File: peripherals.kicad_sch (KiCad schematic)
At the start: 34 parts, among them U2 AT7456E, U3 TXU0304PWR, U4 ICM-42688-P, U5 MT29F2G01ABAGDWB-IT_G, U6 DPS310XTSA1, Y2 27MHz

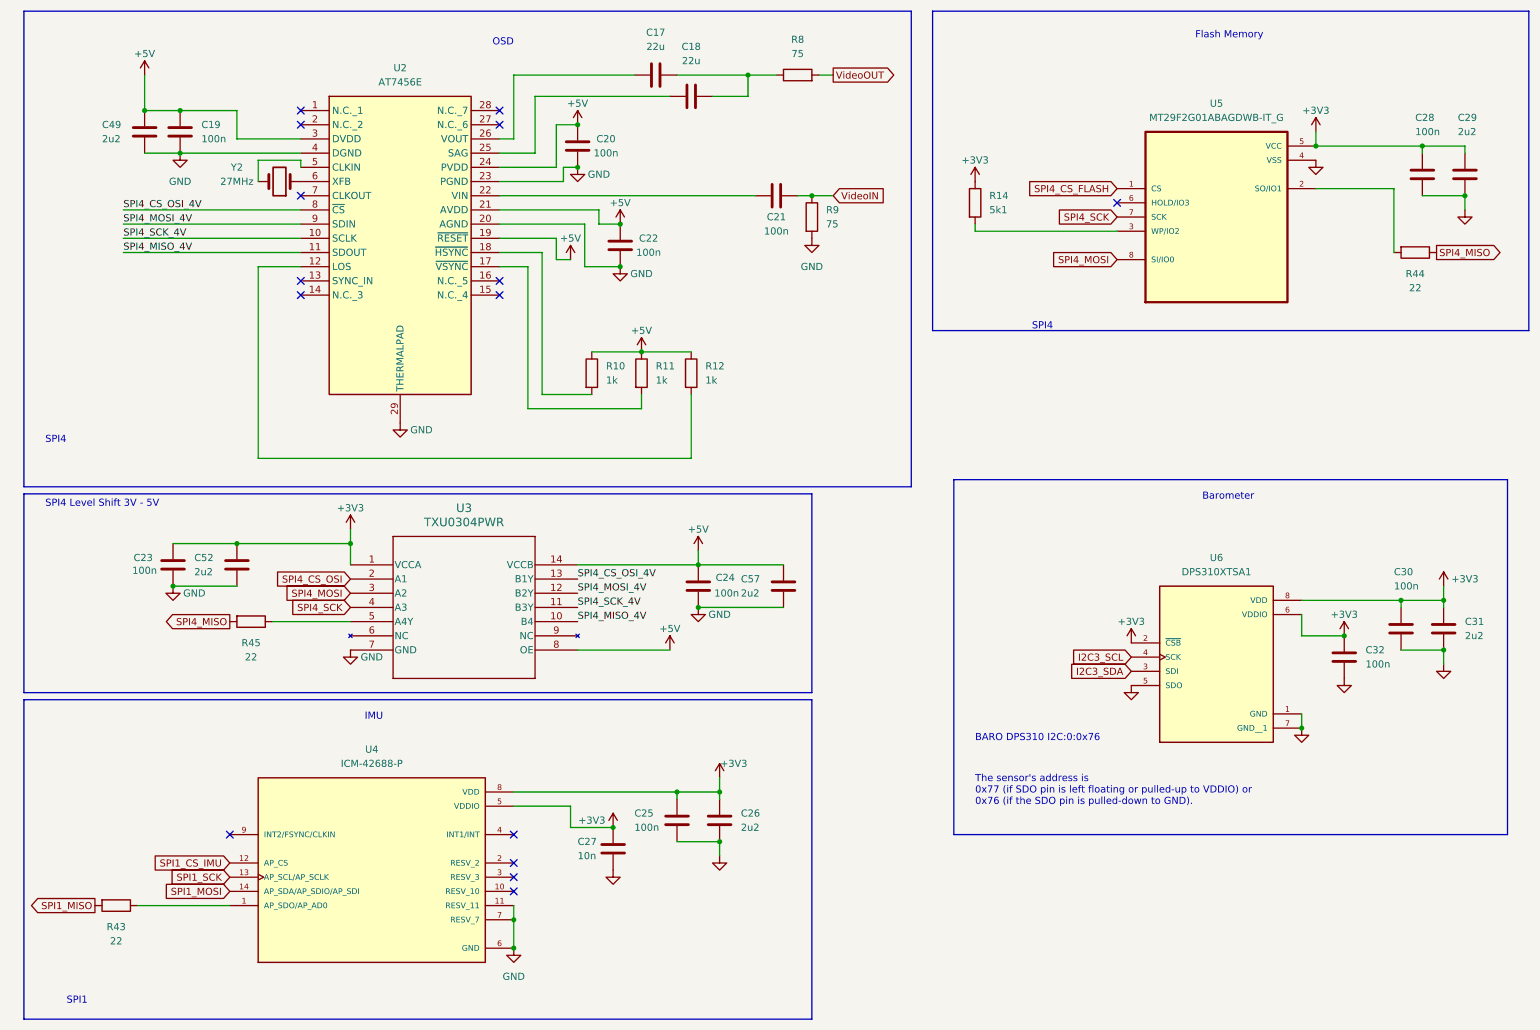
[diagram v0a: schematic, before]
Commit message: change flash to sd flash, cleanup, and reconcile with F405FC
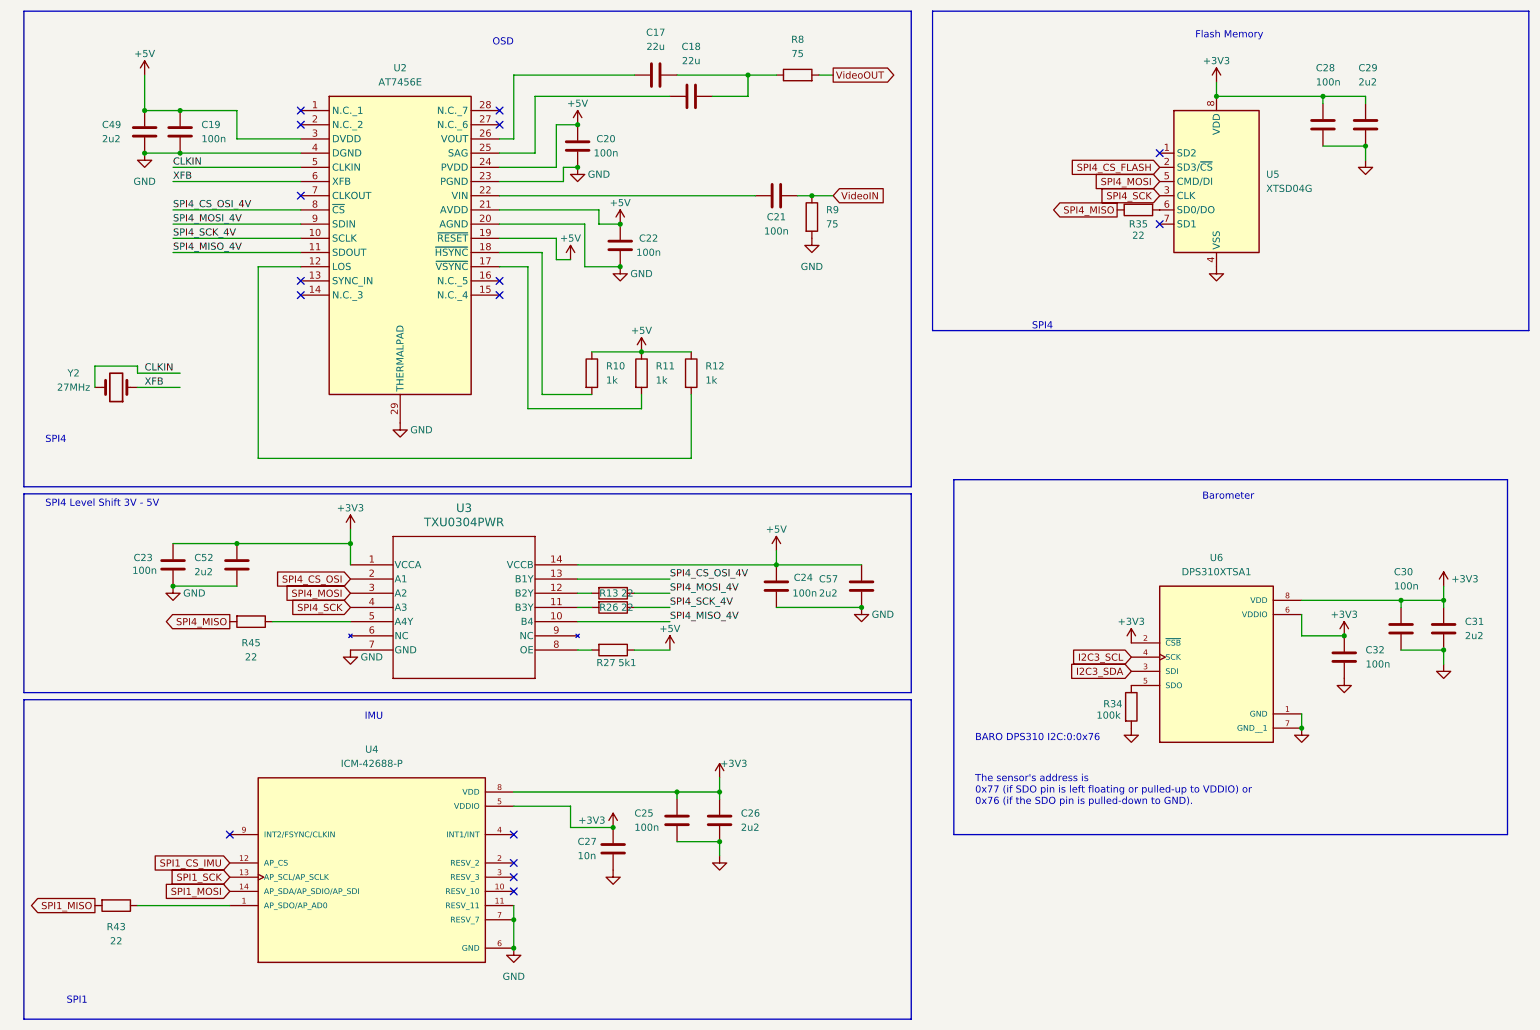
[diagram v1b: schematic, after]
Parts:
- removed R14: 5k1, Project:R_0201_0603Metric, symbol Device:R
- removed R44: 22, Project:R_0201_0603Metric, symbol Device:R
- removed U5: MT29F2G01ABAGDWB-IT_G, Project:SON127P600X800X65-8N, symbol Project_Library:MT29F2G01ABAGDWB-IT_G
- added R13, R26, R35: 22, Project:R_0201_0603Metric, symbol Device:R
- added R27: 5k1, Project:R_0201_0603Metric, symbol Device:R
- added R34: 100k, Project:R_0201_0603Metric, symbol Device:R
- added U5: XTSD04G, Package_LGA:LGA-8_8x6mm_P1.27mm, symbol Memory_Flash:XTSD04G
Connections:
- net +3V3: now also U5.8 (VDD)
- net +5V: now also R27.1; no longer U3.8 (OE)
- net GND: now also R34.2, U5.4 (VSS); no longer U6.5 (SDO)
- net SPI4_CS_FLASH: now also U5.2 (SD3/~{CS})
- net SPI4_MISO: now also R35.1
- net SPI4_MOSI: now also U5.5 (CMD/DI)
- net SPI4_MOSI_4V: now also R13.1; no longer U3.12 (B2Y)
- net SPI4_SCK: now also U5.3 (CLK)
- net SPI4_SCK_4V: now also R26.1; no longer U3.11 (B3Y)
- net XFB: now reaches U2.6 (XFB), Y2.1
- net CLKIN: now reaches U2.5 (CLKIN), Y2.2
- new net: R26.2, U3.11 (B3Y)
- new net: R13.2, U3.12 (B2Y)
- new net: R27.2, U3.8 (OE)
- new net: R34.1, U6.5 (SDO)
- new net: R35.2, U5.6 (SD0/DO)
- no-connect marks 15 -> 16
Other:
- moved on the sheet: C24, C28, C29, C57
